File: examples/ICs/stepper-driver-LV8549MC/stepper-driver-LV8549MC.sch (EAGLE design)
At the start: 8 parts

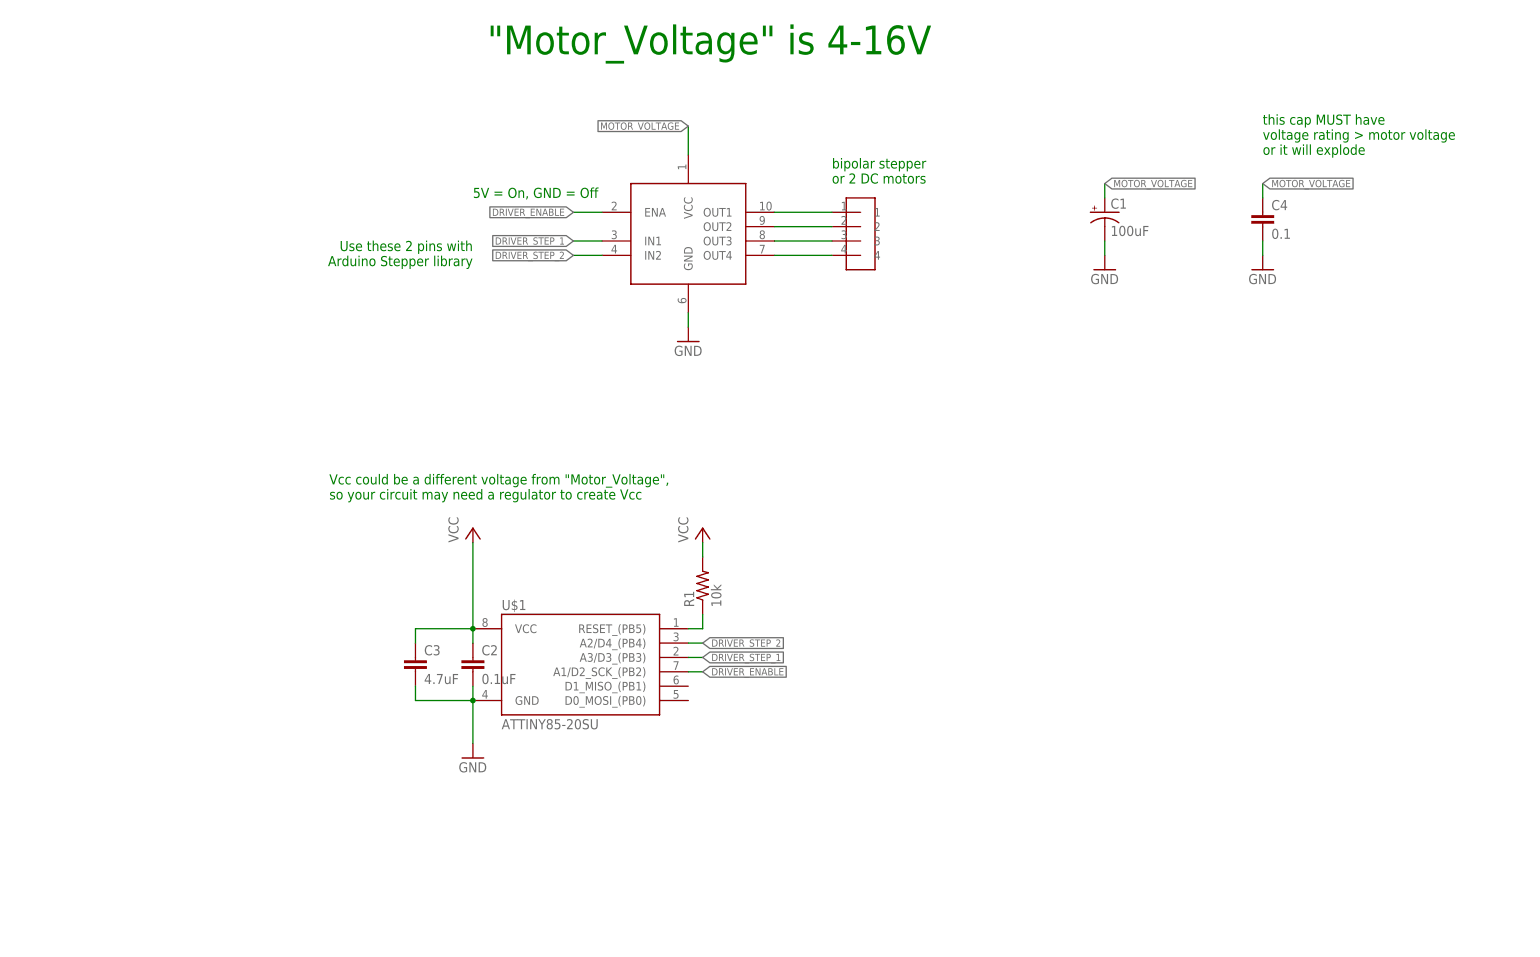
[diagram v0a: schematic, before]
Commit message: makes lipo image easier to read
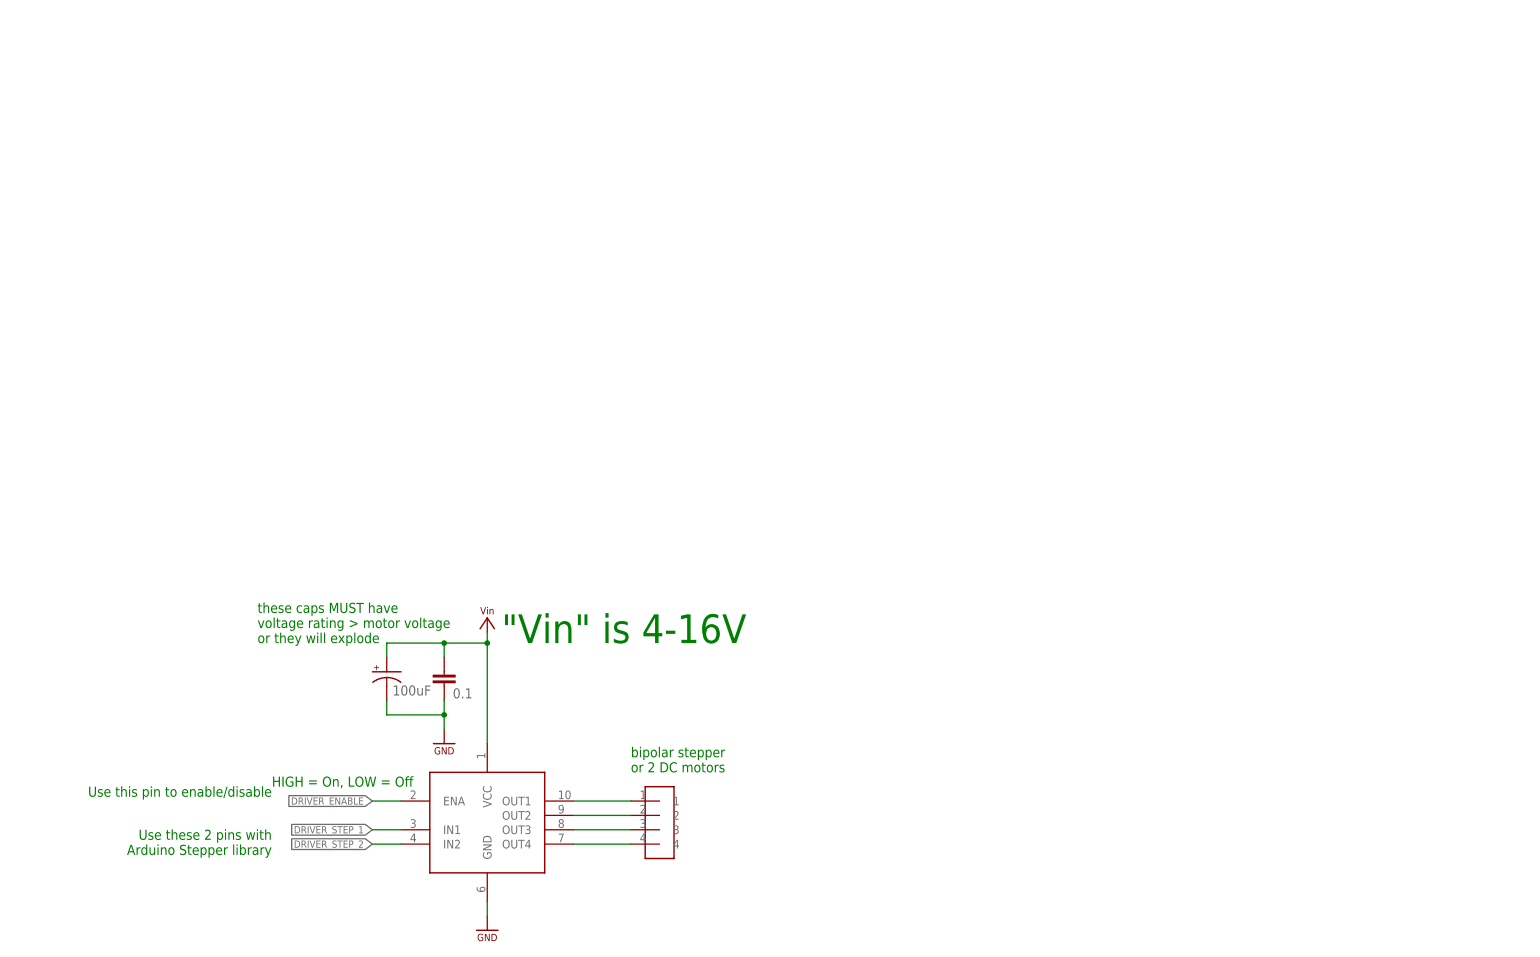
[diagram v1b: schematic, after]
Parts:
- removed C2: 0.1uF, homemade-hardware:CAP0603-CAP
- removed C3: 4.7uF, homemade-hardware:CAP0603-CAP
- removed R1: 10k, homemade-hardware:RESISTOR0603
- removed U$2: HBRIDGE-LV8549MC, homemade-hardware:HBRIDGE-LV8549MC
- removed U$5: HEADER-4, homemade-hardware:HEADER-4
- added U$3: IC_H_BRIDGE_LV8549MC, homemade-hardware:IC_H_BRIDGE_LV8549MC
- U$1: value ATTINY85-20SU -> HEADER-4-HORIZONTAL; device homemade-hardware:ATTINY85-20SU -> homemade-hardware:HEADER-4-HORIZONTAL
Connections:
- removed net MOTOR_VOLTAGE: C1.+, C4.1, U$2.VCC
- removed net N$7: R1.1, U$1.RESET_(PB5)
- removed net VCC: C2.1, C3.1, R1.2, U$1.VCC
- new net VIN: C1.+, C4.1, U$3.VCC
- net DRIVER_ENABLE: now also U$3.ENA; no longer U$1.A1/D2_SCK_(PB2), U$2.ENA
- net DRIVER_STEP_1: now also U$3.IN1; no longer U$1.A3/D3_(PB3), U$2.IN1
- net DRIVER_STEP_2: now also U$3.IN2; no longer U$1.A2/D4_(PB4), U$2.IN2
- net GND: now also U$3.GND; no longer C2.2, C3.2, U$1.GND, U$2.GND
- net N$1: now also U$1.1, U$3.OUT1; no longer U$2.OUT1, U$5.1
- net N$2: now also U$1.2, U$3.OUT2; no longer U$2.OUT2, U$5.2
- net N$3: now also U$1.3, U$3.OUT3; no longer U$2.OUT3, U$5.3
- net N$4: now also U$1.4, U$3.OUT4; no longer U$2.OUT4, U$5.4
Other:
- note added: ""Vin" is 4-16V"
- note added: "HIGH = On, LOW = Off"
- note added: "Use this pin to enable/disable"
- note added: "these caps MUST have voltage rating > motor voltage or they will explode"
- note removed: ""Motor_Voltage" is 4-16V"
- note removed: "5V = On, GND = Off"
- note removed: "Vcc could be a different voltage from "Motor_Voltage", so your circuit may need a regulator to create Vcc"
- note removed: "this cap MUST have voltage rating > motor voltage or it will explode"
